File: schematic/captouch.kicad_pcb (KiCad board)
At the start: 2 copper layers, 26 x 40 mm, 19 parts, among them P1 POWER, P2 PROGRAM, P3 LAMP, Q1 DMN3404L, U1 LD1117S33CTR, U2 MSP430G2553IPW20

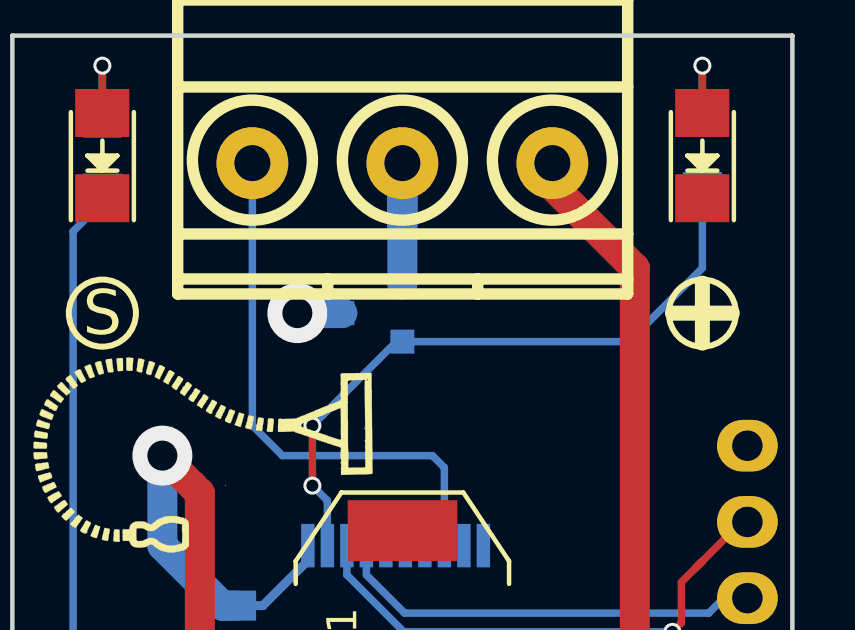
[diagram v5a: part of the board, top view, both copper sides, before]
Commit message: Archived footprints, rev 2 schematic
Fet footprint was wrong. Fixed in this schematic.
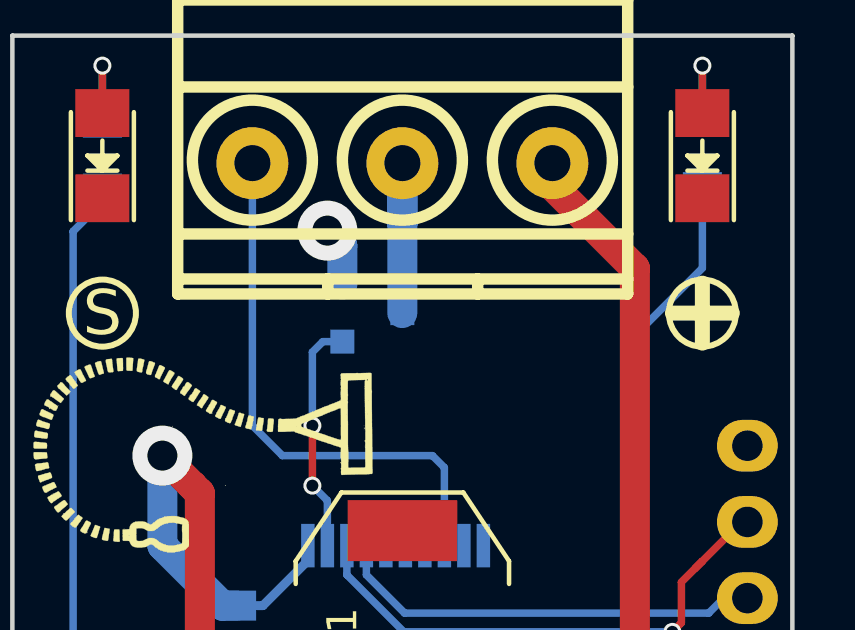
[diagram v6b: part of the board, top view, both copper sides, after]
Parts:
- Q1: footprint TO_SOT_Packages:SOT-23 -> conn:SOT-23
- turned Q1 to 90 degrees
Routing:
- net Net-(Q1-Pad2): track 22.3 -> 14.1 mm
- net Net-(P3-Pad2): track 5.30 -> 6.25 mm
- net GNDREF: track 11.8 -> 12.4 mm
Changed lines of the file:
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@@
   (general
     (links 32)
-    (no_connects 0)
+    (no_connects 4)
     (area 41.4 15.375 87.375001 60.309103)
     (thickness 1.6)
     (drawings 42)
-    (tracks 120)
+    (tracks 121)
     (zones 0)
     (modules 19)
@@
   (title_block
     (title "Captouch lamp control")
-    (date 2016-05-27)
-    (rev 1)
+    (date 2016-06-05)
+    (rev 2)
     (company "Willem Dijkstra <wpd@xs4all.nl>")
   )
@@
     )
   )
-  (module TO_SOT_Packages:SOT-23 (layer B.Cu)
-    (at 64 28.25 270)
-    (descr "SOT-23, Standard")
-    (tags SOT-23)
-    (attr smd)
-    (fp_text reference Q1 (at 0 2.25 270) (layer B.SilkS) hide
-      (effects (font (size 1 1) (thickness 0.15)) (justify mirror))
-    )
-    (fp_text value DMN3404L (at 0 -2.3 270) (layer B.Fab)
-      (effects (font (size 1 1) (thickness 0.15)) (justify mirror))
-    )
-    (fp_line (start -1.65 1.6) (end 1.65 1.6) (layer B.CrtYd) (width 0.05))
-    (fp_line (start 1.65 1.6) (end 1.65 -1.6) (layer B.CrtYd) (width 0.05))
-    (fp_line (start 1.65 -1.6) (end -1.65 -1.6) (layer B.CrtYd) (width 0.05))
-    (fp_line (start -1.65 -1.6) (end -1.65 1.6) (layer B.CrtYd) (width 0.05))
-    (fp_line (start 1.29916 0.65024) (end 1.2509 0.65024) (layer B.SilkS) (width 0.15))
-    (fp_line (start -1.49982 -0.0508) (end -1.49982 0.65024) (layer B.SilkS) (width 0.15))
-    (fp_line (start -1.49982 0.65024) (end -1.2509 0.65024) (layer B.SilkS) (width 0.15))
-    (fp_line (start 1.29916 0.65024) (end 1.49982 0.65024) (layer B.SilkS) (width 0.15))
-    (fp_line (start 1.49982 0.65024) (end 1.49982 -0.0508) (layer B.SilkS) (width 0.15))
-    (pad 1 smd rect (at -0.95 -1.00076 270) (size 0.8001 0.8001) (layers B.Cu B.Paste B.Mask)
-      (net 9 "Net-(P3-Pad2)"))
-    (pad 2 smd rect (at 0.95 -1.00076 270) (size 0.8001 0.8001) (layers B.Cu B.Paste B.Mask)
-      (net 10 "Net-(Q1-Pad2)"))
-    (pad 3 smd rect (at 0 0.99822 270) (size 0.8001 0.8001) (layers B.Cu B.Paste B.Mask)
-      (net 2 GNDREF))
-    (model TO_SOT_Packages_SMD.3dshapes/SOT-23.wrl
-      (at (xyz 0 0 0))
-      (scale (xyz 1 1 1))
-      (rotate (xyz 0 0 0))
-    )
-  )
   (module Resistors_SMD:R_0805 (layer B.Cu)
     (at 75 22.95 270)
@@
       (xy 0.3175 1.5875) (xy 1.051718 1.587204)) (layer B.SilkS) (width 0.01))
   )
+  (module conn:SOT-23 (layer B.Cu)
+    (at 64 28.25 90)
+    (descr "SOT-23, Standard")
+    (tags SOT-23)
+    (attr smd)
+    (fp_text reference Q1 (at 0 2.25 90) (layer B.SilkS) hide
+      (effects (font (size 1 1) (thickness 0.15)) (justify mirror))
+    )
+    (fp_text value DMN3404L (at 0 -2.3 90) (layer B.Fab)
+      (effects (font (size 1 1) (thickness 0.15)) (justify mirror))
+    )
+    (fp_line (start -1.65 1.6) (end 1.65 1.6) (layer B.CrtYd) (width 0.05))
+    (fp_line (start 1.65 1.6) (end 1.65 -1.6) (layer B.CrtYd) (width 0.05))
+    (fp_line (start 1.65 -1.6) (end -1.65 -1.6) (layer B.CrtYd) (width 0.05))
+    (fp_line (start -1.65 -1.6) (end -1.65 1.6) (layer B.CrtYd) (width 0.05))
+    (fp_line (start 1.29916 0.65024) (end 1.2509 0.65024) (layer B.SilkS) (width 0.15))
+    (fp_line (start -1.49982 -0.0508) (end -1.49982 0.65024) (layer B.SilkS) (width 0.15))
+    (fp_line (start -1.49982 0.65024) (end -1.2509 0.65024) (layer B.SilkS) (width 0.15))
+    (fp_line (start 1.29916 0.65024) (end 1.49982 0.65024) (layer B.SilkS) (width 0.15))
+    (fp_line (start 1.49982 0.65024) (end 1.49982 -0.0508) (layer B.SilkS) (width 0.15))
+    (pad 2 smd rect (at -0.95 -1.00076 90) (size 0.8001 0.8001) (layers B.Cu B.Paste B.Mask)
+      (net 10 "Net-(Q1-Pad2)"))
+    (pad 3 smd rect (at 0.95 -1.00076 90) (size 0.8001 0.8001) (layers B.Cu B.Paste B.Mask)
+      (net 2 GNDREF))
+    (pad 1 smd rect (at 0 0.99822 90) (size 0.8001 0.8001) (layers B.Cu B.Paste B.Mask)
+      (net 9 "Net-(P3-Pad2)"))
+    (model TO_SOT_Packages_SMD.3dshapes/SOT-23.wrl
+      (at (xyz 0 0 0))
+      (scale (xyz 1 1 1))
+      (rotate (xyz 0 0 0))
+    )
+  )
   (gr_text GND (at 73.66 32.768) (layer B.SilkS)
     (effects (font (size 1 1) (thickness 0.2)) (justify mirror))
@@
   (segment (start 70 42.25) (end 70.25 42) (width 1) (layer F.Cu) (net 1))
   (segment (start 63.25 47) (end 67.286 42.964) (width 1) (layer F.Cu) (net 1) (status 30))
+  (segment (start 62.99924 27.3) (end 62.99924 25.99924) (width 1) (layer B.Cu) (net 2))
+  (segment (start 62.99924 25.99924) (end 62.5 25.5) (width 1) (layer B.Cu) (net 2))
+  (via (at 62.5 25.5) (size 2) (drill 1) (layers F.Cu B.Cu) (net 2))
   (segment (start 59.5 40) (end 60.45 40) (width 0.3) (layer B.Cu) (net 2))
   (segment (start 60.45 40) (end 61.85 41.4) (width 0.3) (layer B.Cu) (net 2))
@@
   (segment (start 57 41) (end 57 45) (width 1) (layer B.Cu) (net 2))
   (via (at 57 45) (size 2) (drill 1) (layers F.Cu B.Cu) (net 2))
-  (segment (start 63.00178 28.25) (end 61.5 28.25) (width 1) (layer B.Cu) (net 2) (status 10))
-  (via (at 61.5 28.25) (size 2) (drill 1) (layers F.Cu B.Cu) (net 2))
   (segment (start 59.5 38) (end 60.35 38) (width 0.3) (layer B.Cu) (net 3))
   (segment (start 60.35 38) (end 61.85 36.5) (width 0.3) (layer B.Cu) (net 3))
@@
   (segment (start 60 25.017766) (end 60 23.25) (width 0.25) (layer B.Cu) (net 8))
   (segment (start 60 23.25) (end 60 24) (width 0.25) (layer B.Cu) (net 8) (status 30))
-  (segment (start 65.00076 27.3) (end 65.00076 25.25) (width 1) (layer B.Cu) (net 9) (status 10))
+  (segment (start 64.99822 28.25) (end 64.99822 25.25254) (width 1) (layer B.Cu) (net 9))
+  (segment (start 64.99822 25.25254) (end 65.00076 25.25) (width 1) (layer B.Cu) (net 9))
   (segment (start 65.00076 25.25) (end 65.00076 24.00076) (width 1) (layer B.Cu) (net 9) (status 20))
   (segment (start 65 23.25) (end 65 25.24924) (width 1) (layer B.Cu) (net 9) (status 10))
   (segment (start 65 25.24924) (end 65.00076 25.25) (width 1) (layer B.Cu) (net 9))
   (segment (start 65.00076 24.00076) (end 65 24) (width 1) (layer B.Cu) (net 9) (status 30))
-  (segment (start 62 32) (end 64.8 29.2) (width 0.25) (layer B.Cu) (net 10))
-  (segment (start 64.8 29.2) (end 65.00076 29.2) (width 0.25) (layer B.Cu) (net 10))
+  (segment (start 62 32) (end 62 29.54919) (width 0.25) (layer B.Cu) (net 10))
+  (segment (start 62 29.54919) (end 62.34919 29.2) (width 0.25) (layer B.Cu) (net 10))
+  (segment (start 62.34919 29.2) (end 62.99924 29.2) (width 0.25) (layer B.Cu) (net 10))
   (segment (start 62 34) (end 62 32) (width 0.25) (layer F.Cu) (net 10))
   (via (at 62 32) (size 0.6) (drill 0.4) (layers F.Cu B.Cu) (net 10))
@@
   (segment (start 62.5 34.5) (end 62 34) (width 0.25) (layer B.Cu) (net 10))
   (via (at 62 34) (size 0.6) (drill 0.4) (layers F.Cu B.Cu) (net 10))
-  (segment (start 65.00076 29.24924) (end 65.00076 29.2) (width 0.25) (layer B.Cu) (net 10) (status 30))
-  (segment (start 65.00076 29.2) (end 72.55 29.2) (width 0.25) (layer B.Cu) (net 10) (status 10))
   (segment (start 72.55 29.2) (end 75 26.75) (width 0.25) (layer B.Cu) (net 10))
   (segment (start 75 26.75) (end 75 23.9) (width 0.25) (layer B.Cu) (net 10) (status 20))

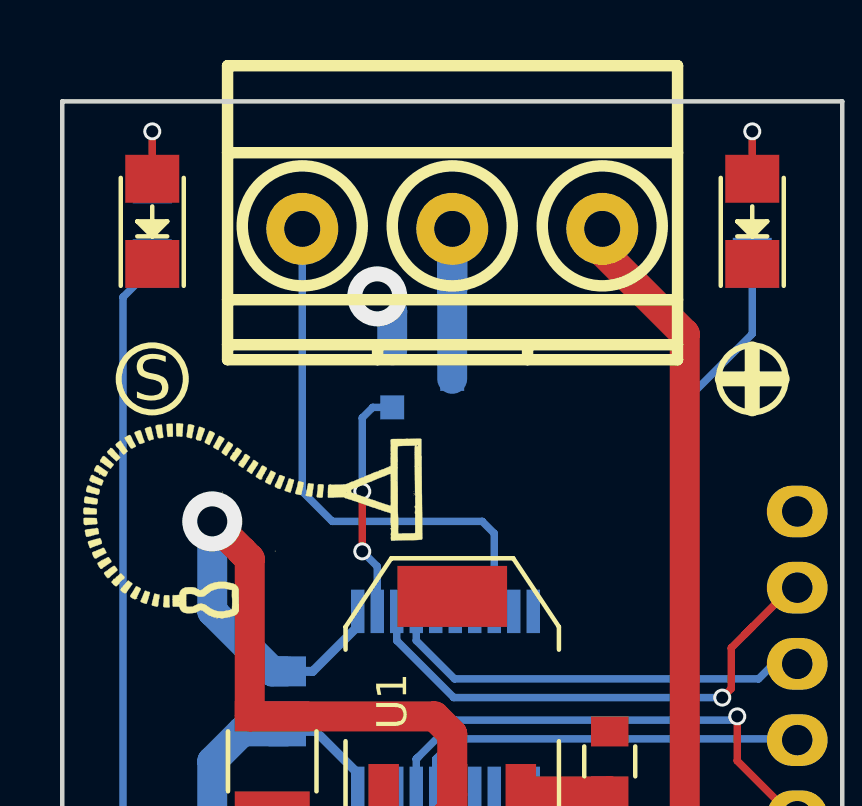
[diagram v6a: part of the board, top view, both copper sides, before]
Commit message: Added high pass filter
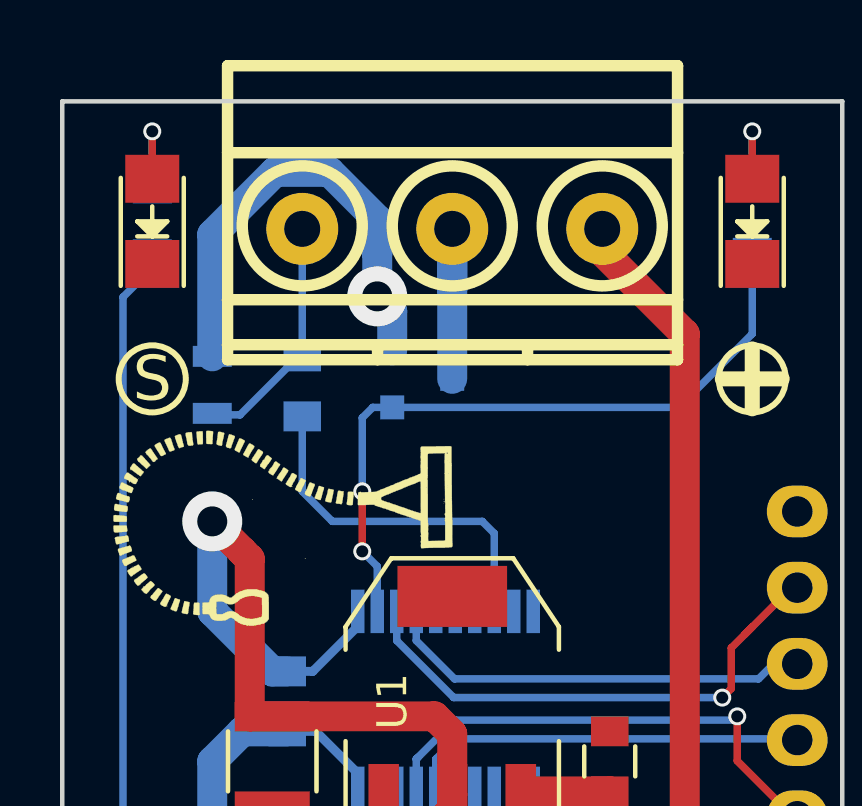
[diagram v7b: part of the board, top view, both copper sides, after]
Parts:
- removed the ? at (58.5, 32.8)
- removed the ? at (56.0, 54.0)
- added   : , logo:lamp, F.Cu at (59.5, 33.0)
- added C4: 470p, Capacitors_SMD:C_0805, B.Cu at (60.0, 28.5)
- added R4: 470k, Resistors_SMD:R_0805, B.Cu at (57.0, 28.4)
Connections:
- P3 pad 3: Net-(P3-Pad3) -> SENSE
- U2 pad 8: Net-(P3-Pad3) -> Net-(C4-Pad1)
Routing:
- net Net-(P3-Pad3): track 19.1 -> 0.00 mm
- net GNDREF: track 12.4 -> 26.0 mm
- net Net-(C4-Pad1): track 0.00 -> 12.1 mm
- net Net-(Q1-Pad2): track 14.1 -> 23.7 mm
- net SENSE: track 0.00 -> 8.81 mm

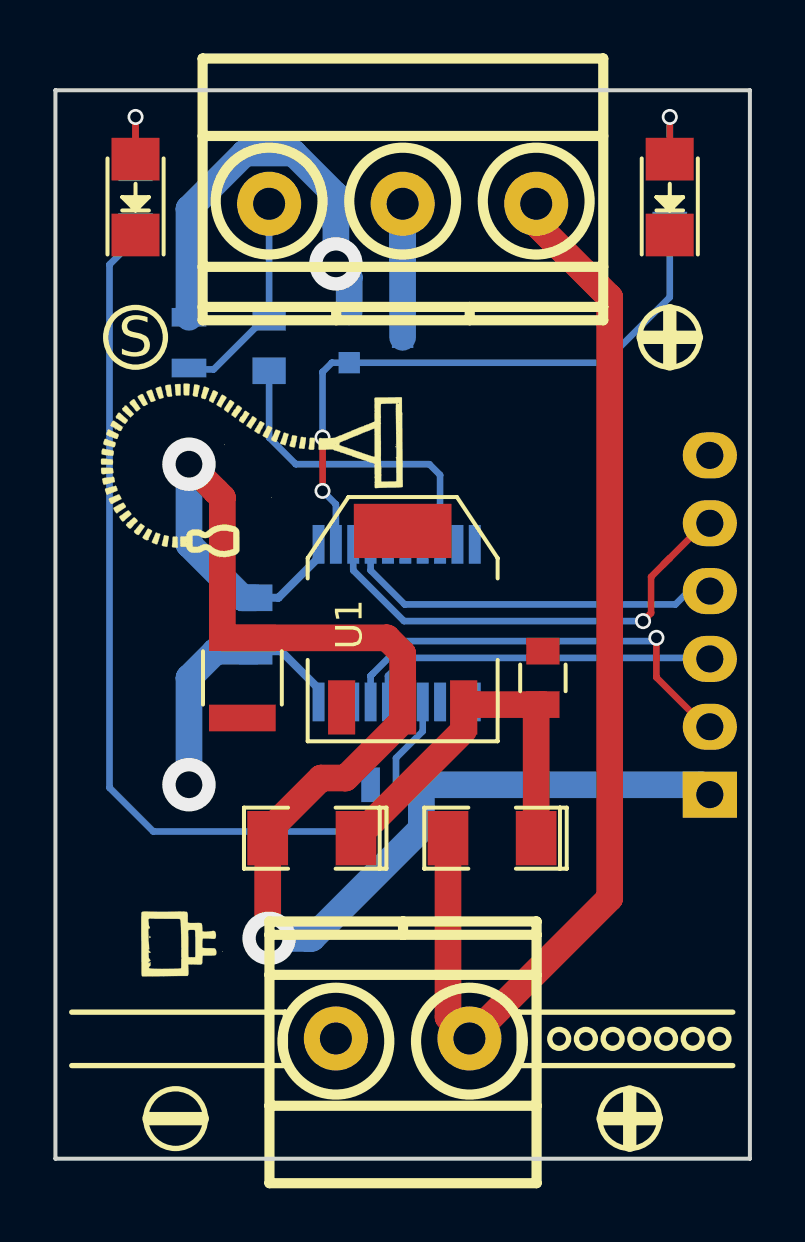
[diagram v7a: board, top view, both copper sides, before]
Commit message: Update schematic to kicad 6
I wanted renders of the schematics, so adjusted all components to
kicad standard components. This way we also get to the associated 3d
models.
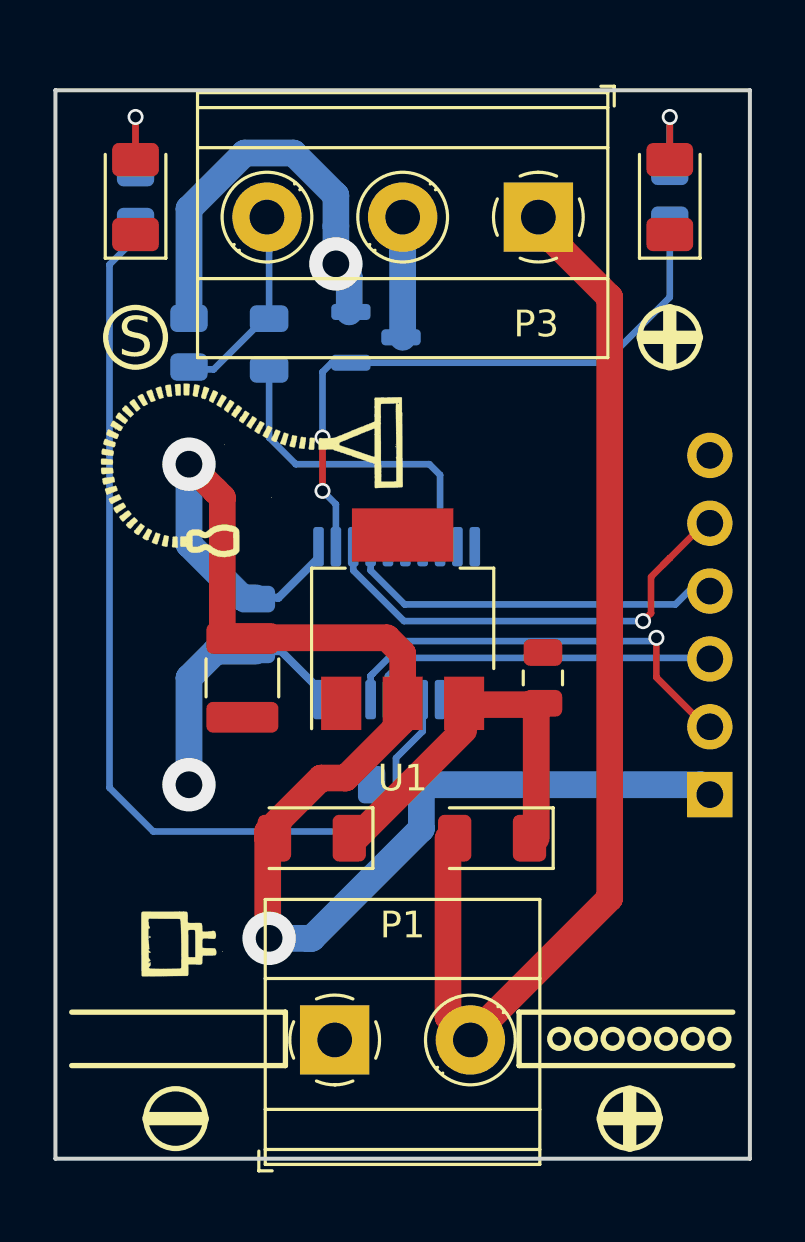
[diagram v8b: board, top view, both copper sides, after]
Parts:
- C1, C3, C4: footprint Capacitors_SMD:C_0805 -> Capacitors_SMD:C_0805_2012Metric
- C2: footprint Capacitors_SMD:C_1210 -> Capacitors_SMD:C_1210_3225Metric
- D1, D2: footprint LEDs:LED_1206 -> LED_SMD:LED_1206_3216Metric
- D3, D4: footprint SMD_Packages:SMD-1206_Pol -> Diode_SMD:D_1206_3216Metric
- P1: footprint conn:P_1,5-2 -> TerminalBlock_Phoenix:TerminalBlock_Phoenix_MKDS-1,5-2-5.08_1x02_P5.08mm_Horizontal
- P2: footprint Pin_Headers:Pin_Header_Angled_1x06 -> Connector_PinSocket_2.54mm:PinSocket_1x06_P2.54mm_Vertical
- P3: footprint conn:P_1,5-3 -> TerminalBlock_Phoenix:TerminalBlock_Phoenix_MKDS-1,5-3-5.08_1x03_P5.08mm_Horizontal
- Q1: footprint conn:SOT-23 -> Package_TO_SOT_SMD:SOT-23
- R1, R2, R3, R4: footprint Resistors_SMD:R_0805 -> Resistors_SMD:R_0805_2012Metric
- U1: value LD1117S33CTR -> LD1117S33TR_SOT223; footprint TO_SOT_Packages:SOT-223 -> SOT:SOT-223
- U2: footprint Housings_SSOP:TSSOP-20_4.4x6.5mm_Pitch0.65mm -> Package_SO:TSSOP-20_4.4x6.5mm_P0.65mm
- moved P3 5.10 mm to (70.1, 23.8)
- moved P1 2.55 mm to (62.5, 54.6)
- turned Q1 to 0 degrees
- turned U1 to 90 degrees
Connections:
- net +3V3 renamed +3.3V
- net /RST renamed /RST
- net Net-(D3-Pad2) renamed +7V
- Q1 pad 1: Net-(P3-Pad2) -> Net-(Q1-Pad1)
- Q1 pad 2: Net-(Q1-Pad2) -> GNDREF
- Q1 pad 3: GNDREF -> Net-(P3-Pad2)
- R2 pad 2: Net-(Q1-Pad2) -> Net-(Q1-Pad1)
- U2 pad 10: (no net) -> unconnected-(U2-Pad10)
- U2 pad 11: (no net) -> unconnected-(U2-Pad11)
- U2 pad 12: (no net) -> unconnected-(U2-Pad12)
- U2 pad 13: (no net) -> unconnected-(U2-Pad13)
- U2 pad 15: (no net) -> unconnected-(U2-Pad15)
- U2 pad 18: (no net) -> unconnected-(U2-Pad18)
- U2 pad 19: (no net) -> unconnected-(U2-Pad19)
- U2 pad 2: Net-(Q1-Pad2) -> Net-(Q1-Pad1)
- U2 pad 5: (no net) -> unconnected-(U2-Pad5)
- U2 pad 6: (no net) -> unconnected-(U2-Pad6)
- U2 pad 7: (no net) -> unconnected-(U2-Pad7)
- U2 pad 9: (no net) -> unconnected-(U2-Pad9)
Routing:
- net Net-(Q1-Pad2): track 23.7 -> 0.00 mm, vias 2 -> 0
- net Net-(Q1-Pad1): track 0.00 -> 23.7 mm, vias 0 -> 2
- net Net-(P3-Pad2): track 6.25 -> 8.25 mm
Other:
- net class Default removed
- net class Power removed
